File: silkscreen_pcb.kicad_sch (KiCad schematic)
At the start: 173 parts, among them J1 USB_C_Receptacle, J2 FH34SRJ-24S-0.5SH_50_, J3 FH34SRJ-6S-0.5SH_50_, J4 FH34SRJ-6S-0.5SH_50_, J5 Conn_01x02, J6 PPPC062LJBN-RC, J7 Micro_SD_Card, Q1 FS8205A, Q3 AO3419, Q4 BSS138, Q5 BSS138, Q6 BSS138, Q7 AO3419, Q8 AO3419, SW1 SW_Push, SW10 SW_Push, SW11 SW_Push, SW2 SW_Push, SW3 SW_Push, SW4 SW_Push, SW5 SW_Push, SW6 SW_Push, SW7 SW_Push, SW8 SW_Push, SW9 SW_Push, U1 TPD4E1U06DBVR, U10 TPS923610DRLR, U11 TP4056-42-ESOP8, U12 74LVC1G04, U13 DS3231MZ, U2 TPS2116DRL, U3 TLV75533PDBV, U4 ESP32-S3-WROOM-1, U5 DW01A, U6 TPD4E1U06DBVR, U7 TPD4E1U06DBVR, U8 TPD4E1U06DBVR, U9 TPD4E1U06DBVR

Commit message: microSD: dual-source push-push footprint (TF PUSH / MEM2075) + doc/BOM sync
- Add project-local microSD_dualsource footprint accepting SHOU HAN TF PUSH
  (LCSC C393941, JLC builds) or GCT MEM2075-00-140-01-A (DigiKey). Built from
  the exact SHOU HAN DXF + GCT .kicad_mod, with FastEDA WRL 3D model. Pinout
  identical to Hirose DM3AT (1-8 signals, 9=shield/GND); replaces the push-pull
  DM3AT on J7. fp-lib-table registers the new library.
- BOM/docs sync to settled parts: J7 push-push (MEM2075 DigiKey / TF PUSH JLC);
  L2 -> VLS252010HBU-4R7M (C413592); U4 -> N16R8; SW1-11 tactiles note TS365ZJ
  (C557598); CR1-3 note SD05C alt; SW6 -> DNP.
- DESIGN_REVIEW: add microSD connector-swap note; fix stale 6.9 nit (SD VDD is
  gated by Q7, not hard-wired; C37 is 1uF).
- THIRD_PARTY: attribute microSD footprint sources + FastEDA WRL model.
- Recolor FH34SRJ 24-pin 3D STEP (placeholder magenta/cyan -> dark plastic +
  silver shell).
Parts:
- J7: footprint Connector_Card:microSD_HC_Hirose_DM3AT-SF-PEJM5 -> microSD_dualsource:microSD_PushPush_TFPUSH-MEM2075
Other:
- note added: "HIGH-Z = USB LOW = BATTERY"
- note added: "Switchover at ~4V"
- note added: "VLS252010HBU-4R7M"
- note removed: "74479325207247"
- note removed: "HIGH = USB LOW = BATTERY"
- note removed: "Switchover at ~3.4V"
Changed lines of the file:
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@@
 		)
 	)
-	(text "HIGH = USB\nLOW = BATTERY"
+	(text "HIGH-Z = USB\nLOW = BATTERY"
 		(exclude_from_sim no)
-		(at 151.384 70.104 0)
+		(at 147.574 62.484 0)
 		(effects
 			(font
@@
 		)
 	)
-	(text "74479325207247"
+	(text "VLS252010HBU-4R7M"
 		(exclude_from_sim no)
 		(at 302.26 234.188 0)
@@
 		)
 	)
-	(text "Switchover at ~3.4V"
+	(text "Switchover at ~4V"
 		(exclude_from_sim no)
 		(at 169.672 42.926 90)
@@
 			)
 		)
-		(property "Footprint" "Connector_Card:microSD_HC_Hirose_DM3AT-SF-PEJM5"
+		(property "Footprint" "microSD_dualsource:microSD_PushPush_TFPUSH-MEM2075"
 			(at 361.95 74.93 0)
 			(effects

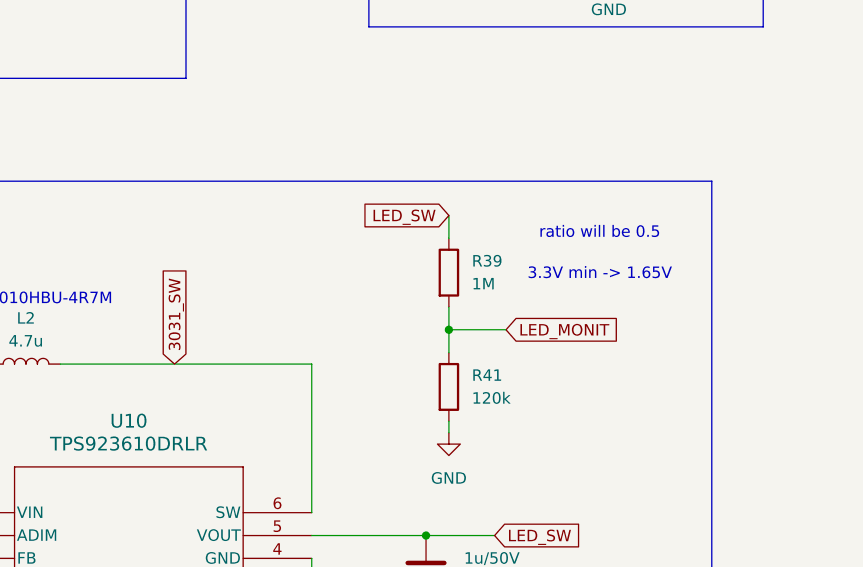
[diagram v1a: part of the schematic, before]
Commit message: Prototype-run release: button re-center, schematic cleanup, doc refresh, as-ordered BOM
Board / schematic:
- Re-center bottom button row (SW2/SW3/SW8/SW9) on the board (was 2.5 mm right
  of center; now 11.5 mm margin each side, 12/13/12 spacing kept).
- Fix stale AP3031-era net name and the LED_MONIT/ADC annotation.

Docs:
- Regenerate full schematic capture (full-capture.png) and per-block images;
  add PCB layout plot (silkscreen_pcb_layout.pdf).
- Remove superseded assets (board-3d-top.png, 00-full-sheet.png,
  18-color-select.png, silkscreen_pcb.pdf) and repoint all README/HARDWARE/
  DESIGN_REVIEW links to the current plots.
- Document SW6 (BOOT/IO0) as DNP + USB-Serial-JTAG download path (HARDWARE 9.3,
  DESIGN_REVIEW); fix the stale 6.9 microSD-VDD nit.

Fabrication:
- Add the as-ordered JLC BOM (production/bom_JLC_upload.csv): clean 4-column
  format with the settled LCSC parts (TS365ZJ tactiles, TF PUSH microSD, SD05C,
  cheaper 22 uF, L2 VLS252010HBU-4R7M) and all DNP components listed for
  completeness (U13 DS3231MZ+, SW6, R43/R45/R58/R66/R72/R74).

This is the design state for the first JLCPCB prototype run.
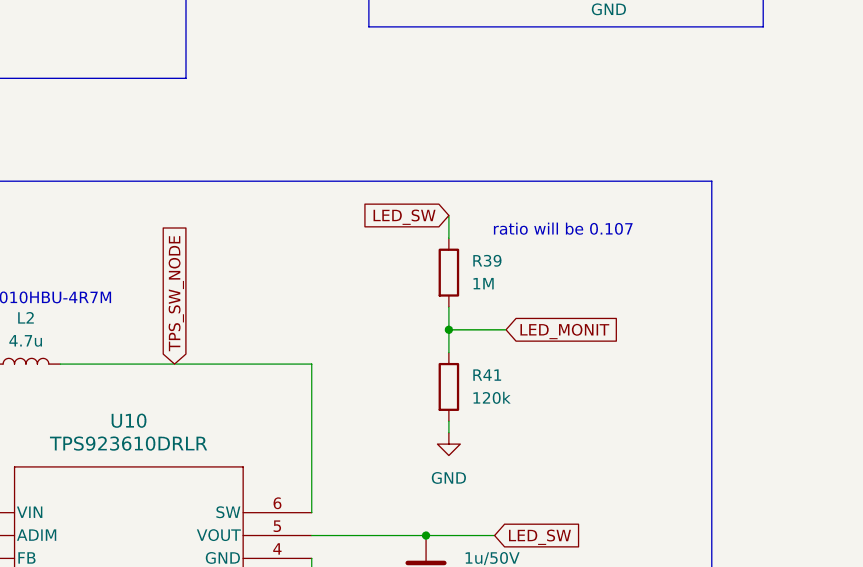
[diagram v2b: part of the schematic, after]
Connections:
- net 3031_SW renamed TPS_SW_NODE
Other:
- note added: "ratio will be 0.107"
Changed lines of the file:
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@@
 		)
 	)
-	(text "ratio will be 0.5"
+	(text "ratio will be 0.107"
 		(exclude_from_sim no)
-		(at 366.014 226.822 0)
-		(effects
-			(font
-				(size 1.27 1.27)
-			)
-		)
-	)
-	(text "3.3V min -> 1.65V"
-		(exclude_from_sim no)
-		(at 366.014 231.394 0)
+		(at 361.95 226.568 0)
 		(effects
 			(font
@@
 		)
 	)
-	(global_label "3031_SW"
+	(global_label "TPS_SW_NODE"
 		(shape input)
 		(at 318.77 241.3 90)
@@
 		)
 		(property "Intersheetrefs" "${INTERSHEET_REFS}"
-			(at 318.77 229.8483 90)
+			(at 318.77 225.1916 90)
 			(effects
 				(font

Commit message: Post-review revision: reverse-battery CE gate, 10 uH L2, layout fixes, optimized BOM
Board / schematic:
- Reverse-battery fix ("Fix 4"): TP4056 CE is no longer tied to USB_VBUS. It is
  driven from 3V3 through Q2 (P-FET), enabled by a cell-polarity detector
  referenced to raw B- (Q9 BSS138, R79 100k, R80/R81/R82 1M). A reversed cell
  keeps the charger disabled; idle cost on battery is ~3.4 uA.
- Q4 (EPD charge-pump switch) -> IRLML6346TRPBF. R37 -> 15 ohm (~13.3 mA LED
  ceiling, under the panel's 15 mA limit).
- L2 -> 10 uH (TI characterizes the TPS923610 only with 10 uH; modelled ~6-7 mA
  less battery draw at every brightness). Q2/Q3/Q7/Q8 -> AO3401A.
  CR1 (VBUS TVS) value -> SMF6.5CA.
- Layout: +16 GND stitching vias, solid zone connections on the power/sense
  ground pads, C2 moved to the TP4056 VCC pin, 3V3 feed to the module re-routed.
- microSD dual-source footprint: locating holes become 1.50 mm-tall slots and a
  MEM2075 keep-out outline is drawn, so both the TF PUSH and the GCT MEM2075 seat.
- DRC: 0 unconnected. Known open items in this snapshot: CR1 footprint still
  SOD-323 (SMF6.5CA needs Diode_SMD:D_SMF), L2 value on the PCB not yet synced
  from the schematic, SW6 not yet flagged DNP.

Docs:
- HARDWARE.md rewritten against the current netlist (SD/ESD pin mapping, RTC,
  charger, Fix 4, frontlight limits, component appendix).
- DESIGN_REVIEW.md: decided set recorded (Fix 4 with simulation results and the
  rejected alternatives, Q4/R37/J7 applied, L2, CR1, standard-build DNP policy);
  evidence, scripts and results under docs/audit-2026-09-16/.

Fabrication:
- BOM.md rewritten: netlist-derived standard build (162 fitted, 10 DNP), swap
  rationale, cost model, review of the earlier price-maxed sheet.
- production/bom_JLC_upload_v4_optimized.csv (standard JLCPCB upload, every part
  checked against JLC's library) and bom_JLC_upload_v3.csv (brand-conservative).
- fabrication/BOM_handbuild_digikey.csv: hand-build list of prime parts.
- fabrication/par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
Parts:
- added Q2: AO3401A, Package_TO_SOT_SMD:SOT-23_Handsoldering, symbol Transistor_FET:IRLML6402
- added Q9: BSS138, Package_TO_SOT_SMD:SOT-23, symbol Transistor_FET:BSS138
- added R79: 100k, Resistor_SMD:R_0603_1608Metric_Pad0.98x0.95mm_HandSolder, symbol Device:R
- added R80, R81, R82: 1M, Resistor_SMD:R_0603_1608Metric_Pad0.98x0.95mm_HandSolder, symbol Device:R
- CR1: value TSD05CDYFR -> SMF6.5CA
- L2: value 4.7u -> 10u
- Q3, Q7, Q8: value AO3419 -> AO3401A
- Q4: value BSS138 -> IRLML6346TRPBF
- R37: value 13.3 -> 15
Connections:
- net 3V3: now also Q2.2 (S), R81.2
- net B+: now also R79.1
- net B-: now also Q9.2 (S), R80.1
- net GND: now also R82.1
- net USB_VBUS: no longer U11.8 (CE)
- new net: Q9.1 (G), R79.2, R80.2
- new net CE: Q2.3 (D), R82.2, U11.8 (CE)
- new net DET_NODE: Q2.1 (G), Q9.3 (D), R81.1
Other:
- note added: "VLS252012HBX-100M-1"
- note removed: "50V"
- note removed: "VLS252010HBU-4R7M"
- moved on the sheet: J5

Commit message: Battery-path widening, 0805 jumper, C9/L1/R14 updates, JLC ordering guide
- B+/B-/P+ traces widened to 0.4 mm; R27 zero-ohm jumper 0603 -> 0805
  (LCSC C17477, prime Yageo RC0805JR-070RL); part_fields and BOMs updated
- L1 47 uH (Laird TYS5040470M-10 / Sunltech C206267), R14 2.2 ohm,
  C9 4.7 uF, Q1 manufacturer corrected
- Regenerated JLC production set (gerbers, CPL, BOM) and plots
- README: step-by-step JLCPCB upload flow and optional/base part groups
- Second full review (docs/audit-2026-09-18), refreshed images and docs
- Trimmed sym/fp library tables; pruned stale exports
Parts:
- C1: LCSC (none) -> C1588; MPN (none) -> CL10B102KB8NNNC; Manufacturer (none) -> Samsung Electro-Mechanics
- C10, C12: LCSC (none) -> C19666; MPN (none) -> CL10A475KO8NNNC; Manufacturer (none) -> Samsung Electro-Mechanics
- C11, C13, C14, C15, C16, C17: LCSC (none) -> C513770; MPN (none) -> CL21A475KBQNNNE; Manufacturer (none) -> Samsung Electro-Mechanics
- C18, C19, C20: LCSC (none) -> C28323; MPN (none) -> CL21B105KBFNNNE; Manufacturer (none) -> Samsung Electro-Mechanics
- C2, C3: LCSC (none) -> C19702; MPN (none) -> CL10A106KP8NNNC; Manufacturer (none) -> Samsung Electro-Mechanics
- C21, C22, C25, C26, C37, C5, C8: LCSC (none) -> C15849; MPN (none) -> CL10A105KB8NNNC; Manufacturer (none) -> Samsung Electro-Mechanics
- C23, C27, C28, C29: LCSC (none) -> C1604; MPN (none) -> CL10B222KB8NNNC; Manufacturer (none) -> Samsung Electro-Mechanics
- C24, C30, C31, C33, C36, C7: LCSC (none) -> C14663; MPN (none) -> CC0603KRX7R9BB104; Manufacturer (none) -> Yageo
- C32, C4, C6: LCSC (none) -> C20416420; MPN (none) -> CL21A226MAQNNNE; Manufacturer (none) -> Samsung Electro-Mechanics
- C9: value 1u/50V -> 4.7u/50V; LCSC (none) -> C513770; MPN (none) -> CL21A475KBQNNNE; Manufacturer (none) -> Samsung Electro-Mechanics
- CR1: footprint Diode_SMD:D_SOD-323_HandSoldering -> Diode_SMD:D_SMF; LCSC (none) -> C19077501; MPN (none) -> SMF6.5CA; Manufacturer (none) -> Littelfuse
- CR2, CR3: LCSC (none) -> C5299440; MPN (none) -> TSD05CDYFR; Manufacturer (none) -> Texas Instruments
- D2: LCSC (none) -> C28310439; MPN (none) -> LTST-C150KRKT; Manufacturer (none) -> Lite-On
- D3: LCSC (none) -> C19077543; MPN (none) -> SMAJ26A; Manufacturer (none) -> Littelfuse
- D4, D5, D6: LCSC (none) -> C8598; MPN (none) -> 1N5819HW-7-F; Manufacturer (none) -> Diodes Incorporated
- D8: LCSC (none) -> C42370512; MPN (none) -> PESD2IVN-UX; Manufacturer (none) -> Nexperia
- F1: LCSC (none) -> C269106; MPN (none) -> 0805L100WR; Manufacturer (none) -> Littelfuse
- J1: LCSC (none) -> C7095263; MPN (none) -> USB4085-GF-A; Manufacturer (none) -> GCT
- J2: LCSC (none) -> C324726; MPN (none) -> FH34SRJ-24S-0.5SH(50); Manufacturer (none) -> Hirose
- J3, J4: LCSC (none) -> C224194; MPN (none) -> FH34SRJ-6S-0.5SH(50); Manufacturer (none) -> Hirose
- J5: LCSC (none) -> C48579993; MPN (none) -> S2B-PH-K-S(LF)(SN); Manufacturer (none) -> JST
- J6: LCSC (none) -> C5333437; MPN (none) -> PPPC062LJBN-RC; Manufacturer (none) -> Sullins
- J7: LCSC (none) -> C393941; MPN (none) -> MEM2075-00-140-01-A; Manufacturer (none) -> GCT
- L1: value 22u -> 47uH; footprint srn3010C-100m:IND_SRN3010C-100M -> Inductor_SMD:L_APV_ANR5040; LCSC (none) -> C206267; MPN (none) -> TYS5040470M-10; Manufacturer (none) -> Laird
- L2: LCSC (none) -> C88532; MPN (none) -> VLS252012HBX-100M-1; Manufacturer (none) -> TDK
- Q1: LCSC (none) -> C2830320; MPN (none) -> FS8205A; Manufacturer (none) -> EVVOSEMI
- Q2, Q3, Q7, Q8: LCSC (none) -> C15127; MPN (none) -> AO3401A; Manufacturer (none) -> Alpha & Omega Semiconductor
- Q4: LCSC (none) -> C67276; MPN (none) -> IRLML6346TRPBF; Manufacturer (none) -> Infineon
- Q5, Q6, Q9: LCSC (none) -> C7420339; MPN (none) -> BSS138LT1G; Manufacturer (none) -> onsemi
- R1, R10, R12, R39, R49, R50, R57, R80, R81, R82: LCSC (none) -> C22935; MPN (none) -> RC0603FR-071ML; Manufacturer (none) -> Yageo
- R11: LCSC (none) -> C22790; MPN (none) -> RC0603FR-0712KL; Manufacturer (none) -> Yageo
- R13, R15, R28, R4, R5, R53, R54, R55, R56, R62, R7, R72, R8, R9: LCSC (none) -> C25804; MPN (none) -> RC0603FR-0710KL; Manufacturer (none) -> Yageo
- R14: value 3 -> 2.2; LCSC (none) -> C112307; MPN (none) -> RC0603FR-072R2L; Manufacturer (none) -> Yageo
- R16, R78: LCSC (none) -> C21190; MPN (none) -> RC0603FR-071KL; Manufacturer (none) -> Yageo
- R17: LCSC (none) -> C22807; MPN (none) -> RC0603FR-07150KL; Manufacturer (none) -> Yageo
- R18: LCSC (none) -> C23189; MPN (none) -> RC0603FR-075K6L; Manufacturer (none) -> Yageo
- R19: LCSC (none) -> C4184; MPN (none) -> RC0603FR-0720KL; Manufacturer (none) -> Yageo
- R2, R3: LCSC (none) -> C23186; MPN (none) -> RC0603FR-075K1L; Manufacturer (none) -> Yageo
- R20, R67: LCSC (none) -> C23206; MPN (none) -> RC0603FR-0756KL; Manufacturer (none) -> Yageo
- R21, R22, R23, R24, R25, R26, R29, R30, R31, R32, R33, R34, R65, R68, R69: LCSC (none) -> C23140; MPN (none) -> RC0603FR-0733RL; Manufacturer (none) -> Yageo
- R27: footprint Resistor_SMD:R_0603_1608Metric_Pad0.98x0.95mm_HandSolder -> Resistor_SMD:R_0805_2012Metric_Pad1.20x1.40mm_HandSolder; LCSC (none) -> C17477; MPN (none) -> RC0805JR-070RL; Manufacturer (none) -> Yageo
- R35: LCSC (none) -> C4216; MPN (none) -> RC0603FR-0733KL; Manufacturer (none) -> Yageo
- R36: LCSC (none) -> C23231; MPN (none) -> RC0603FR-0768KL; Manufacturer (none) -> Yageo
- R37: LCSC (none) -> C22810; MPN (none) -> RC0603FR-0715RL; Manufacturer (none) -> Yageo
- R38: LCSC (none) -> C23024; MPN (none) -> RC0603FR-07300KL; Manufacturer (none) -> Yageo
- R40, R51, R70, R75, R76, R77, R79: LCSC (none) -> C25803; MPN (none) -> RC0603FR-07100KL; Manufacturer (none) -> Yageo
- R41: LCSC (none) -> C25808; MPN (none) -> RC0603FR-07120KL; Manufacturer (none) -> Yageo
- R42, R43, R44, R45, R46, R52, R58, R66, R73, R74: LCSC (none) -> C21189; MPN (none) -> RC0603JR-070RL; Manufacturer (none) -> Yageo
- R47, R48: LCSC (none) -> C4190; MPN (none) -> RC0603FR-072K2L; Manufacturer (none) -> Yageo
- R59: LCSC (none) -> C22975; MPN (none) -> RC0603FR-072KL; Manufacturer (none) -> Yageo
- R6: LCSC (none) -> C23162; MPN (none) -> RC0603FR-074K7L; Manufacturer (none) -> Yageo
- R60, R61, R63, R64: LCSC (none) -> C22775; MPN (none) -> RC0603FR-07100RL; Manufacturer (none) -> Yageo
- R71: LCSC (none) -> C31850; MPN (none) -> RC0603FR-0722KL; Manufacturer (none) -> Yageo
- SW1, SW10, SW11, SW2, SW3, SW4, SW5, SW7, SW8, SW9: LCSC (none) -> C557598; MPN (none) -> MJTP1117; Manufacturer (none) -> APEM
- SW6: MPN (none) -> MJTP1243; Manufacturer (none) -> APEM; now not fitted
- U1, U6, U7, U8, U9: LCSC (none) -> C19829453; MPN (none) -> TPD4E1U06DBVR; Manufacturer (none) -> Texas Instruments
- U10: LCSC (none) -> C52919131; MPN (none) -> TPS923610DRLR; Manufacturer (none) -> Texas Instruments
- U11: LCSC (none) -> C16581; MPN (none) -> TP4056-42-ESOP8; Manufacturer (none) -> NanJing Top Power (TOPPOWER)
- U12: LCSC (none) -> C53185133; MPN (none) -> 74LVC1G04GV,125; Manufacturer (none) -> Nexperia
- U13: LCSC (none) -> C107410; MPN (none) -> DS3231MZ+TRL; Manufacturer (none) -> Analog Devices
- U2: LCSC (none) -> C3235557; MPN (none) -> TPS2116DRLR; Manufacturer (none) -> Texas Instruments
- U3: LCSC (none) -> C404027; MPN (none) -> TLV75533PDBVR; Manufacturer (none) -> Texas Instruments
- U4: LCSC (none) -> C2913202; MPN (none) -> ESP32-S3-WROOM-1-N16R8; Manufacturer (none) -> Espressif Systems
- U5: LCSC (none) -> C351410; MPN (none) -> DW01A; Manufacturer (none) -> Fortune Semiconductor
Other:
- note added: "TYS5040470M-10"
- note removed: "VLS3012HBX-220M"

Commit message: Final-review revision: DW01A filters, J6 fuse, alternate RTC, sleep-current ladder, doc and fab refresh
Design (Rev 1.0, content current to 2026-09-21):
- DW01A: R83 100R supply filter with C7 on the pin side, C34 2.2n on CS
- F2 0805L075WR PPTC in series with J6 pin 12; CR3 now on the fused net
- U14 RV-8263-C7 alternate RTC footprint (DNP) with a project symbol library
- USB_STAT ladder rescaled x10 (R70 1M, R17 2M, R67 510k, R71 200k, C23 0.1u)
  and R57 10M: about 15 uA less sleep current
- R15 1M, C2 25 V part, 22 uF to Basic C45783, R14 to Basic C22939
- H6 mounting hole, H5 moved, single 5.30 x 1.10 mm neck slot, wider VBUS trunk
- Silkscreen: GitHub QR now points at silkscreen-pcb, battery warning at the
  cut line, display part number GDEQ0426T82-FT01C, LED current 13.3 mA
- Symbol fields corrected (AO3401A, IRLML6346, 1N5819HW, TVS, ESD arrays,
  connectors); local simulation-model paths removed

Fabrication:
- production/ regenerated with the Fabrication Toolkit and verified against
  the saved board; bom_JLC_upload_v4_optimized.csv renamed jlc_bom.csv,
  v3 removed; other-fab files regenerated
- part_fields.csv, BOM.md and the hand-build BOM updated

Docs:
- README rewritten as a JLCPCB ordering guide for beginners, with a real
  quote, glossary, configuration groups and the other-fab position
- HARDWARE.md: firmware contract, enclosure dimensions, new ladder levels,
  battery-protection and mounting notes; schematic screenshots, PDFs, board
  renders and a STEP model regenerated
- DESIGN_REVIEW.md status banner; simulations/ and the old de-link parts
  sheet removed
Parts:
- added C34: 2.2n, Capacitor_SMD:C_0603_1608Metric_Pad1.08x0.95mm_HandSolder, symbol Device:C
- added F2: 0805L075WR, Fuse:Fuse_0805_2012Metric_Pad1.15x1.40mm_HandSolder, symbol Device:Polyfuse
- added H6: MountingHole_Pad, MountingHole:MountingHole_2.2mm_M2_DIN965_Pad_TopBottom, symbol Mechanical:MountingHole_Pad
- added R83: 100, Resistor_SMD:R_0603_1608Metric_Pad0.98x0.95mm_HandSolder, symbol Device:R
- added U14: RV-8263-C7, Package_SON:MicroCrystal_C7_SON-8_1.5x3.2mm_P0.9mm, symbol RV-8263-C7:RV-8263-C7
- C18, C19: value 1u -> 1u/50V
- C2: value 10u -> 10u/25V; LCSC C19702 -> C96446; MPN CL10A106KP8NNNC -> CL10A106MA8NRNC
- C23: value 2.2n -> 0.1u; LCSC C1604 -> C14663; MPN CL10B222KB8NNNC -> CC0603KRX7R9BB104; Manufacturer Samsung Electro-Mechanics -> Yageo
- C24, C31: value 100n -> 0.1u
- C32, C4, C6: LCSC C20416420 -> C45783; MPN CL21A226MAQNNNE -> GRM21BR61E226ME44L; Manufacturer Samsung Electro-Mechanics -> Murata Electronics
- R14: LCSC C112307 -> C22939
- R15: value 10k -> 1M; LCSC C25804 -> C22935; MPN RC0603FR-0710KL -> RC0603FR-071ML
- R17: value 150k -> 2M; LCSC C22807 -> C22976; MPN RC0603FR-07150KL -> RC0603FR-072ML
- R57: value 1M -> 10M; LCSC C22935 -> C7250; MPN RC0603FR-071ML -> RC0603FR-0710ML
- R67: value 56k -> 510k; LCSC C23206 -> C23192; MPN RC0603FR-0756KL -> RC0603FR-07510KL
- R70: value 100k -> 1M; LCSC C25803 -> C22935; MPN RC0603FR-07100KL -> RC0603FR-071ML
- R71: value 22k -> 200k; LCSC C31850 -> C25811; MPN RC0603FR-0722KL -> RC0603FR-07200KL
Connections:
- net 3V3: now also U14.5 (VDD)
- net B-: now also C34.2
- net GND: now also H6.1, U14.2 (VSS), U14.3 (CLKOE)
- net I2C_SCL: now also U14.7 (SCL)
- net I2C_SDA: now also U14.8 (SDA)
- net P+: now also F2.2, R83.2; no longer C7.1, CR3.1 (I/O), J6.12, U5.5 (VCC)
- net at R16.2, U5.2 (CS): now also C34.1
- new net: C7.1, R83.1, U5.5 (VCC)
- new net P+_FUSE: CR3.1 (I/O), F2.1, J6.12
- no-connect marks 15 -> 18
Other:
- note added: "0.1u cap placed near ESP32"
- note added: "Explanation for Q8 (EEVblog DW01/8205A thread):"
- note added: "LED lit when USB is plugged in 1.5mA at 2.0Vf (5 − 2.0)/0.0015 ≈ 2 kΩ"
- note added: "Only populate one, or none at all. DS3231 is more stocked RV8263 is cheaper"
- note added: "USB / CHARGE STATUS ADC DIVIDER NOTE: Monitors TPS2116 ST and TP4056 CHRG/STDBY via single ADC pin (USB_STAT). Draw: 1.1 uA on battery, < 3 uA on USB. High-Z node + C23: ~0.5 s to settle. PRIMARY OPERATIONAL STATES: 1) Discharging / Unplugged (VIN2 Active): ~2.20 V [Window: 1.80 V - 2.60 V] 2) Plugged in & Actively Charging: ~1.11 V [Window: 0.80 V - 1.35 V] 3) Plugged in & Fully Charged (Done): 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"
- note removed: "Explanation for Q8:"
- note removed: "LED lit when plugged in 2.5mA at 2.0Vf (5 − 2.0)/0.0015 ≈ 2 kΩ"
- note removed: "USB / CHARGE STATUS ADC DIVIDER NOTE: Monitors TPS2116 ST and TP4056 CHRG/STDBY via single ADC pin (USB_STAT). Max continuous current draw: < 30 uA. PRIMARY OPERATIONAL STATES: 1) Discharging / Unplugged (VIN2 Active): ~1.98 V [Window: 1.70 V - 2.20 V] 2) Plugged in & Actively Charging: ~1.18 V [Window: 1.00 V - 1.35 V] 3) Plugged in & Fully Charged (Done): ~0.59 V [Window: 0.50 V - 0.70 V] 4) Pl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"
- moved on the sheet: C30, C7, H5, R16, R63, R64, SW11, SW6, U13
